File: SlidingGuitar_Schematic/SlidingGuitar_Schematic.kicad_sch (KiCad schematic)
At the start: 4 parts, among them J1 Barrel_Jack, M1 Motor_DC, U1 DRV8871DDA

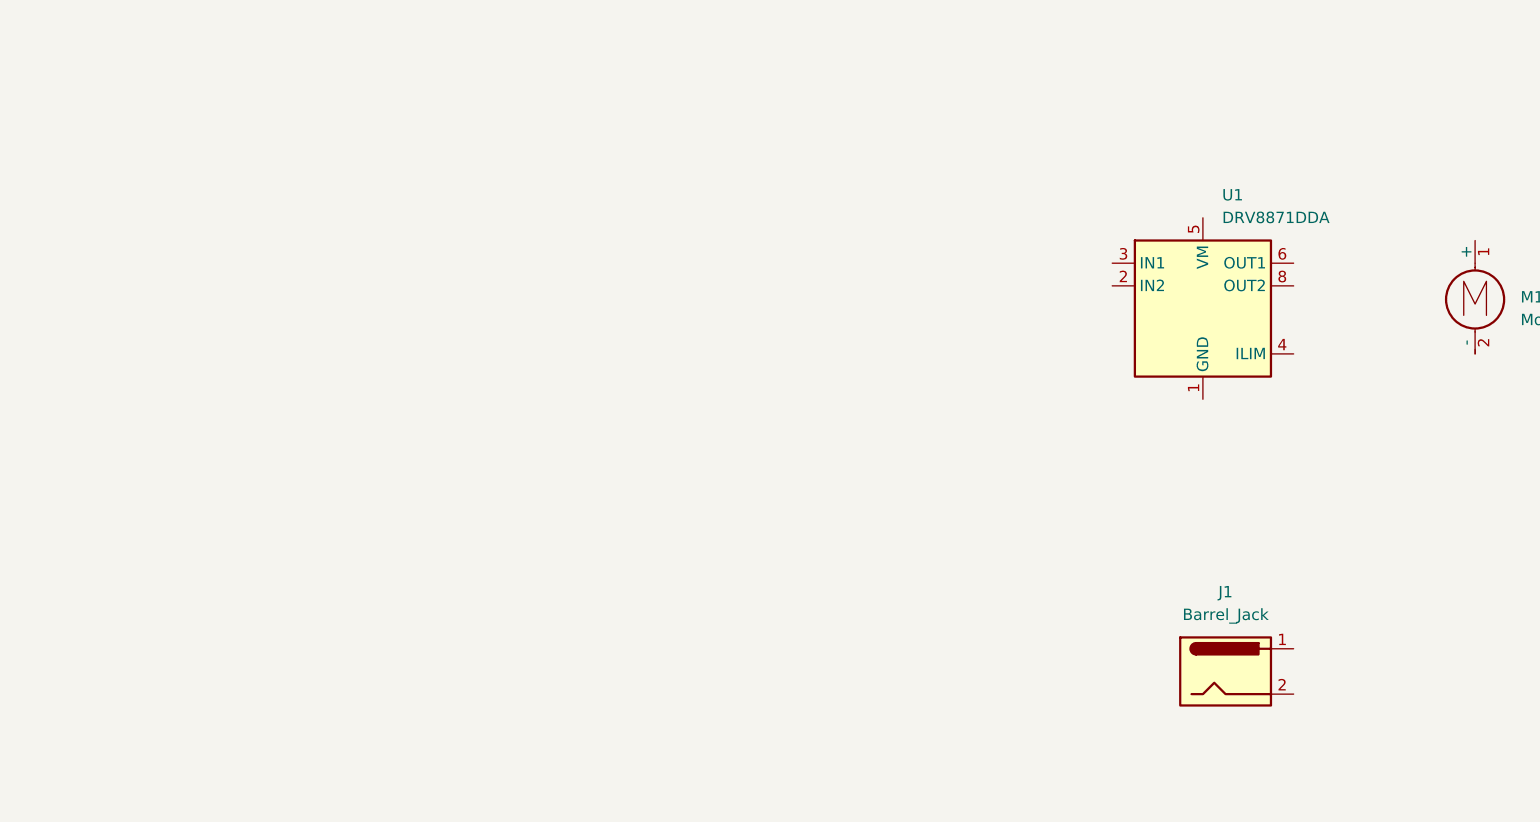
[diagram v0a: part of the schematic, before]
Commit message: Added LM386 circuit
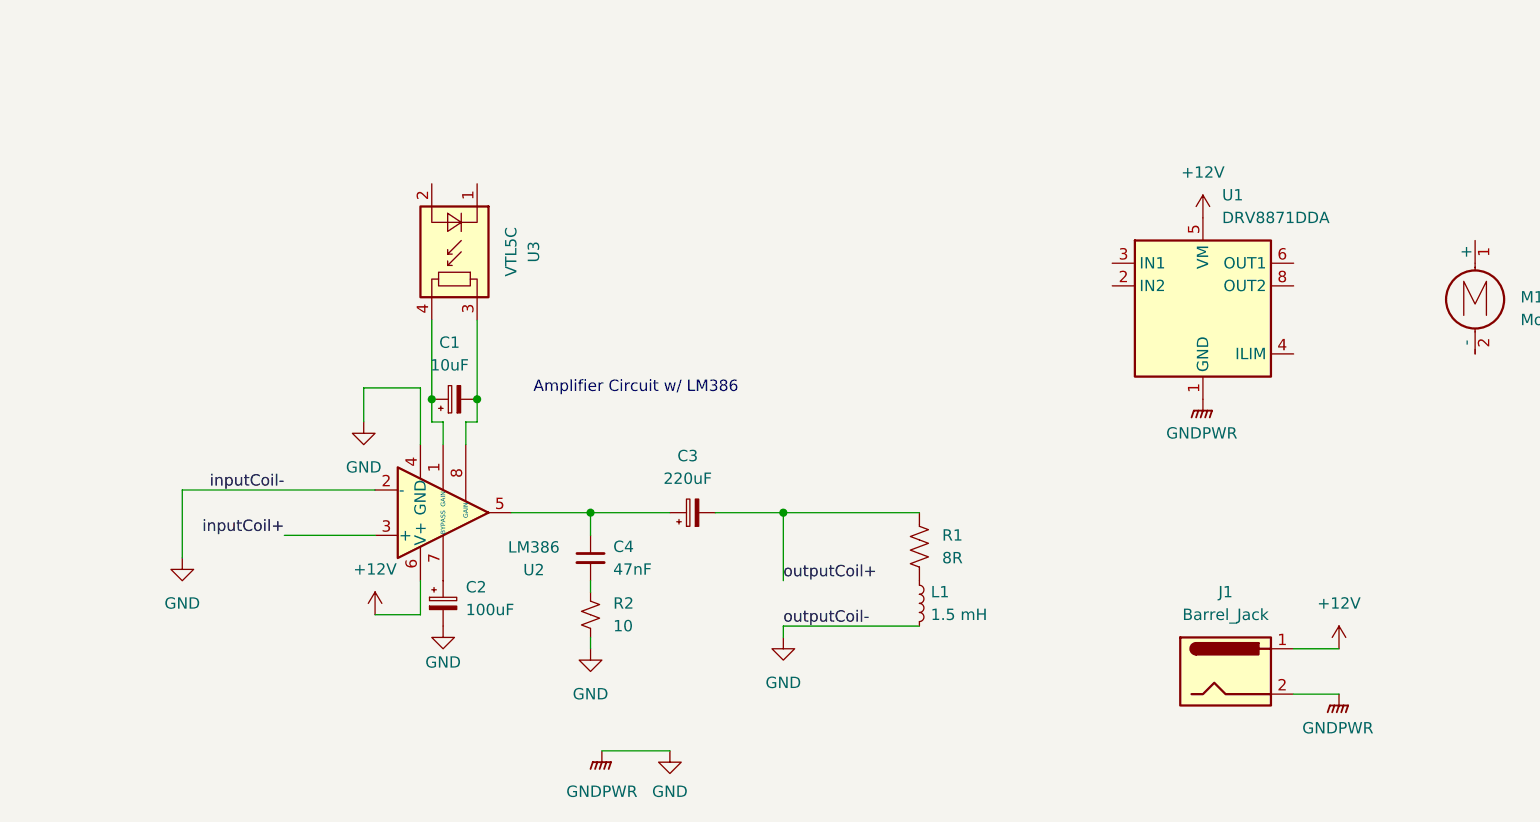
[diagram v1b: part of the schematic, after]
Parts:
- added C1: 10uF, symbol Device:C_Polarized_Small
- added C2: 100uF, symbol Device:C_Polarized_Small
- added C3: 220uF, symbol Device:C_Polarized_Small
- added C4: 47nF, symbol Device:C_Small
- added L1: 1.5 mH, symbol Device:L_Small
- added R1: 8R, symbol Device:R_US
- added R2: 10, symbol Device:R_Small_US
- added U2: LM386, Package_DIP:DIP-8_W7.62mm, symbol Amplifier_Audio:LM386
- added U3: VTL5C, OptoDevice:PerkinElmer_VTL5Cx2, symbol Isolator:VTL5C
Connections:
- net +12V: now reaches J1.1
- net +12V: now also U1.5 (VM), U2.6 (V+)
- net GND: now reaches J1.2
- net GND: now also U1.1 (GND), U1.7 (GND), U1.9 (GND), C2.2, L1.2, R2.2, U2.2 (-), U2.4 (GND)
- new net: C3.1, C4.1, U2.5
- new net: C4.2, R2.1
- new net: C1.1, U2.1 (GAIN), U3.4
- new net: C2.1, U2.7 (BYPASS)
- new net: C1.2, U2.8 (GAIN), U3.3
- new net: L1.1, R1.2
- new net inputCoil+: U2.3 (+)
- new net outputCoil+: C3.2, R1.1
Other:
- note added: "Amplifier Circuit w/ LM386"

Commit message: Add lock file for SlidingGuitar_Schematic to track PCB design session
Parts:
- removed C1: 10uF, symbol Device:C_Polarized_Small
- removed C2: 100uF, symbol Device:C_Polarized_Small
- removed C3: 220uF, symbol Device:C_Polarized_Small
- removed C4: 47nF, symbol Device:C_Small
- removed L1: 1.5 mH, symbol Device:L_Small
- removed R2: 10, symbol Device:R_Small_US
- removed U2: LM386, Package_DIP:DIP-8_W7.62mm, symbol Amplifier_Audio:LM386
- removed U3: VTL5C, OptoDevice:PerkinElmer_VTL5Cx2, symbol Isolator:VTL5C
- added C31, C32: 100uF, Capacitor_THT:CP_Radial_D8.0mm_P5.00mm, symbol Device:C_Polarized
- added J10: MotorDriver, Connector_PinHeader_2.54mm:PinHeader_1x04_P2.54mm_Vertical, symbol Connector_Generic:Conn_01x04
- added J11: MotorEncoder, Connector_PinHeader_2.54mm:PinHeader_1x04_P2.54mm_Vertical, symbol Connector_Generic:Conn_01x04
- added J4: 12VPowerSupply, Connector_PinHeader_2.54mm:PinHeader_1x02_P2.54mm_Vertical, symbol Connector_Generic:Conn_01x02
- added J9: AudioJack2, symbol Connector_Audio:AudioJack2
- added R20: 3R3, Resistor_THT:R_Axial_DIN0207_L6.3mm_D2.5mm_P7.62mm_Horizontal, symbol Device:R_US
- J1: footprint (none) -> Connector_BarrelJack:BarrelJack_Horizontal
- R1: value 8R -> 3R3; footprint (none) -> Resistor_THT:R_Axial_DIN0207_L6.3mm_D2.5mm_P7.62mm_Horizontal
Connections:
- net +12V: now also J4.1 (Pin_1), R20.1; no longer U1.5 (VM)
- net GND: now also C31.2, C32.2, J4.2 (Pin_2); no longer U1.1 (GND), U1.7 (GND), U1.9 (GND)
- net at M1.1 (+): now also U1.6 (OUT1)
- net at M1.2 (-): now also U1.8 (OUT2)
- net GNDA: now reaches A1.20 (AGND)
- net +3.3VA: now reaches A1.21 (3V3_A)
- net D24: now reaches A1.31 (SAI2_MCLK)
- net D24: now also J11.3 (Pin_3)
- net D25: now reaches A1.32 (SAI2_SD_B)
- net D25: now also J11.4 (Pin_4)
- net D27: now reaches A1.34 (SAI2_FS)
- net D27: now also J10.3 (Pin_3)
- net D28: now reaches A1.35 (SAI2_SCK)
- net D28: now also J10.4 (Pin_4)
- net +3.3VP: now reaches A1.38 (3V3_D)
- net +3.3VP: now also J10.1 (Pin_1), J11.1 (Pin_1)
- net at A1.39 (VIN): now also R1.2, C31.1
- net D3: now reaches A1.4 (SD_DATA_1)
- net GNDD: now reaches A1.40 (DGND)
- net GNDD: now also J10.2 (Pin_2), J11.2 (Pin_2)
- net D4: now reaches A1.5 (SD_DATA_0)
- net D5: now reaches A1.6 (SD_CMD)
- net D6: now reaches A1.7 (SD_CLK)
- net D7: now reaches A1.8 (SPI1_CS)
- net D8: now reaches A1.9 (SPI1_SCK)
- net outputCoil+: no longer names the net of R1.1
- net outputCoil+: now also C32.1, R20.2
- new net: U1.1 (GND), U1.7 (GND), U1.9 (GND)
- new net Pickup+: J9.T
- new net Pickup-: J9.S
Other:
- added sheet E-Bow Circuit (untitled.kicad_sch)
- added sheet E-Bow Circuit1 (untitled.kicad_sch)
- added sheet E-Bow Circuit2 (untitled.kicad_sch)
- added sheet E-Bow Circuit3 (untitled.kicad_sch)
- added sheet E-Bow Circuit4 (untitled.kicad_sch)
- added sheet E-Bow Circuit5 (untitled.kicad_sch)
- note added: "+ G 1 2"
- note added: "Audio in is a placeholder for the time being; it is possible there will be multiplexing going on"
- note removed: "Amplifier Circuit w/ LM386"
- moved on the sheet: A1, J1, M1, U1
